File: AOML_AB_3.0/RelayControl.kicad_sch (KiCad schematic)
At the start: 52 parts, among them IC1 CD4043BDR, IC2 CD4043BDR, J5 Conn_01x03, K1 TX2-L2-5V, K10 TX2-L2-5V, K11 TX2-L2-5V, K13 TX2-L2-5V, K2 TX2-L2-5V, K3 TX2-L2-5V, K4 TX2-L2-5V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

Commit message: New reorganization on relay drivers and microcontroller pins
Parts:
- removed TP5: B, TestPoint:TestPoint_Pad_1.0x1.0mm, symbol Connector:TestPoint
- removed TP5: C, TestPoint:TestPoint_Pad_1.0x1.0mm, symbol Connector:TestPoint
- removed TP5: A, TestPoint:TestPoint_Pad_1.0x1.0mm, symbol Connector:TestPoint
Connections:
- net Reset1: now also U5.10 (O7); no longer U5.12 (O5)
- net relay_cal_cont: now also RN3.4 (R3), U5.4 (I4); no longer RN3.6 (R5), U5.3 (I3)
- net relay_cal_res: now also RN3.7 (R6), U5.5 (I5); no longer RN3.5 (R4), U5.4 (I4)
- net relay_gnd_cond: now also RN3.8 (R7), U5.3 (I3); no longer RN3.7 (R6), U5.2 (I2)
- net relay_reset1: now also RN1.6 (R5), U5.7 (I7); no longer RN3.4 (R3), U5.5 (I5)
- net relay_reset2: now also RN3.5 (R4); no longer RN3.3 (R2)
- net relay_reset3: now also RN3.6 (R5); no longer RN3.2 (R1)
- net relay_xbt1: now also RN1.5 (R4), U5.6 (I6); no longer RN1.9 (R8), U5.1 (I1)
- net relay_xbt2: now also RN1.7 (R6), U5.5 (I5); no longer RN1.8 (R7), U5.2 (I2)
- net relay_xbt3: now also RN1.4 (R3), U5.4 (I4); no longer RN1.7 (R6), U5.3 (I3)
- net relay_xbt4: now also RN1.8 (R7), U5.3 (I3); no longer RN1.6 (R5), U5.4 (I4)
- net relay_xbt5: now also RN1.3 (R2), U5.2 (I2); no longer RN1.5 (R4), U5.5 (I5)
- net relay_xbt6: now also RN1.2 (R1), U5.1 (I1); no longer RN1.4 (R3), U5.6 (I6)
- net relay_xbt7: now also RN3.2 (R1), U5.1 (I1); no longer RN1.3 (R2), U5.7 (I7)
- net relay_xbt8: now also RN3.3 (R2), U5.2 (I2); no longer RN3.8 (R7), U5.1 (I1)
- net at K13.6 (-_1): now also U5.12 (O5); no longer U5.13 (O4)
- net at K11.6 (-_1): now also U5.13 (O4); no longer U5.14 (O3)
- net at K10.6 (-_1), K9.6 (-_1): now also U5.14 (O3); no longer U5.15 (O2)
- net at K8.6 (-_1): now also U5.15 (O2); no longer U5.16 (O1)
- net at K7.6 (-_1): now also U5.16 (O1); no longer U5.10 (O7)
- no-connect marks 27 -> 26

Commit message: PCB finished, next BOM
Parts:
- RN2, RN4: Digikey https://www.digikey.com/en/products/detail/yageo/YC124-JR-0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 -> https://www.digikey.com/en/products/detail/yageo/YC164-JR-1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
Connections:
- no-connect marks 26 -> 27
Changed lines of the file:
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@@
   (no_connect (at 119.38 111.76))
   (no_connect (at 149.86 251.46))
+  (no_connect (at 54.61 180.34))
   (no_connect (at 149.86 111.76))
   (no_connect (at 119.38 219.71))
@@
       (effects (font (size 1.27 1.27)) hide)
     )
-    (property "Digikey" "https://www.digikey.com/en/products/detail/yageo/YC124-JR-0710KL/1005019" (at 311.15 222.25 0)
+    (property "Digikey" "https://www.digikey.com/en/products/detail/yageo/YC164-JR-1310KL/17023153?s=N4IgTCBcDaIJ4GMCMA2ALAWgFYCcNIGYkAGAawBsQBdAXyA" (at 311.15 222.25 0)
       (effects (font (size 1.27 1.27)) hide)
     )
@@
       (effects (font (size 1.27 1.27)) hide)
     )
-    (property "Digikey" "https://www.digikey.com/en/products/detail/yageo/YC124-JR-0710KL/1005019" (at 311.15 135.89 0)
+    (property "Digikey" "https://www.digikey.com/en/products/detail/yageo/YC164-JR-1310KL/17023153?s=N4IgTCBcDaIJ4GMCMA2ALAWgFYCcNIGYkAGAawBsQBdAXyA" (at 311.15 135.89 0)
       (effects (font (size 1.27 1.27)) hide)
     )

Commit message: PCB finished, BOM finished
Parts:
- K1, K10, K11, K13, K2, K3, K4, K5, K7, K8, K9: Digikey (none) -> https://www.digikey.com/en/products/detail/panasonic-electr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; Manufacturer_Name Panasonic -> (none); Manufacturer_Part_Number TX2-L2-5V -> (none); Mouser Part Number 769-TX2-L2-5V -> (none); Mouser Price/Stock https://www.mouser.co.uk/ProductDetail/Panasonic-Industrial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 -> (none)

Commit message: PCB finished ready to order (no fiducials for assembly), BOM finished
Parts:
- IC1, IC2: Cost (none) -> 0.49; Part (none) -> CD4043BDR
- J5: Cost (none) -> 1.27; Part (none) -> 0436500315
- K1, K10, K11, K13, K2, K3, K4, K5, K7, K8, K9: Cost (none) -> 3.61; Part (none) -> TX2-L2-5V
- K6: Cost (none) -> 3.61; Digikey (none) -> https://www.digikey.com/en/products/detail/panasonic-electr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; Manufacturer_Name Panasonic -> (none); Manufacturer_Part_Number TX2-L2-5V -> (none); Mouser Part Number 769-TX2-L2-5V -> (none); Mouser Price/Stock https://www.mouser.co.uk/ProductDetail/Panasonic-Industrial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 -> (none); Part (none) -> TX2-L2-5V
- R1: Cost (none) -> 0.1; Part (none) -> RC0805FR-10330RL
- R10: Cost (none) -> 38.87; Part (none) -> Y14535K00000V9L
- R11: Cost (none) -> 0.1; Part (none) -> CFR-25JR-52-15K
- RN1, RN3: Cost (none) -> 0.14; Part (none) -> YC158TJR-0710KL
- RN2, RN4: Cost (none) -> 0.1; Part (none) -> YC164-JR-1310KL
- U10, U11, U12, U13, U14, U15, U16, U17: Cost (none) -> 1.28; Part (none) -> TLP170AM(TPL,E
- U5: Cost (none) -> 0.46; Part (none) -> ULN2003ADR

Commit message: PCB v2 started to make changes after meeting w/P.P & Z.B. - XBT connectors, AXR ABC and MUX GPS Tx
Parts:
- J5: footprint Molex_3x1_0436500315:CON_436500315_MOL -> CUI_3x1_connector:CUI_TBP02R2-381-03BE; Cost 1.27 -> 0.58; Digikey https://www.digikey.com/en/products/detail/molex/0436500315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 -> https://www.digikey.com/en/products/detail/cui-devices/TBP0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; Part 0436500315 -> TBP02R2-381-03BE
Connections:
- net XBT1_A: now also J5.3 (Pin_3); no longer J5.1 (Pin_1)
- net XBT1_C: now also J5.1 (Pin_1); no longer J5.3 (Pin_3)
- net XBT2_A: now also J5.3 (Pin_3); no longer J5.1 (Pin_1)
- net XBT2_C: now also J5.1 (Pin_1); no longer J5.3 (Pin_3)
- net XBT3_A: now also J5.3 (Pin_3); no longer J5.1 (Pin_1)
- net XBT3_C: now also J5.1 (Pin_1); no longer J5.3 (Pin_3)
- net XBT4_A: now also J5.3 (Pin_3); no longer J5.1 (Pin_1)
- net XBT4_C: now also J5.1 (Pin_1); no longer J5.3 (Pin_3)
- net XBT5_A: now also J5.3 (Pin_3); no longer J5.1 (Pin_1)
- net XBT5_C: now also J5.1 (Pin_1); no longer J5.3 (Pin_3)
- net XBT6_A: now also J5.3 (Pin_3); no longer J5.1 (Pin_1)
- net XBT6_C: now also J5.1 (Pin_1); no longer J5.3 (Pin_3)
- net XBT7_A: now also J5.3 (Pin_3); no longer J5.1 (Pin_1)
- net XBT7_C: now also J5.1 (Pin_1); no longer J5.3 (Pin_3)
- net XBT8_A: now also J5.3 (Pin_3); no longer J5.1 (Pin_1)
- net XBT8_C: now also J5.1 (Pin_1); no longer J5.3 (Pin_3)

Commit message: New version v3, in assembly process and noting changes for next revision
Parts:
- removed RN1, RN3: 10k, Resistor_network-10k:SMT_JR-0710KL_YAG, symbol Device:R_Network08
- added RN1, RN3: 746X101103JP, Network_resistor_10k_bussed:746X101103JP-3, symbol Network_resistor_10k_bussed:746X101103JP
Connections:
- net GND: now also RN1.10, RN1.5, RN3.10, RN3.5
- net relay_cal_cont: now also RN3.1
- net relay_cal_res: now also RN3.6
- net relay_gnd_cond: now also RN3.2
- net relay_reset1: now also RN1.7
- net relay_reset2: now also RN3.8
- net relay_reset3: now also RN3.7
- net relay_xbt1: now also RN1.8
- net relay_xbt2: now also RN1.6
- net relay_xbt3: now also RN1.1
- net relay_xbt4: now also RN1.2
- net relay_xbt5: now also RN1.3
- net relay_xbt6: now also RN1.4
- net relay_xbt7: now also RN3.4
- net relay_xbt8: now also RN3.3

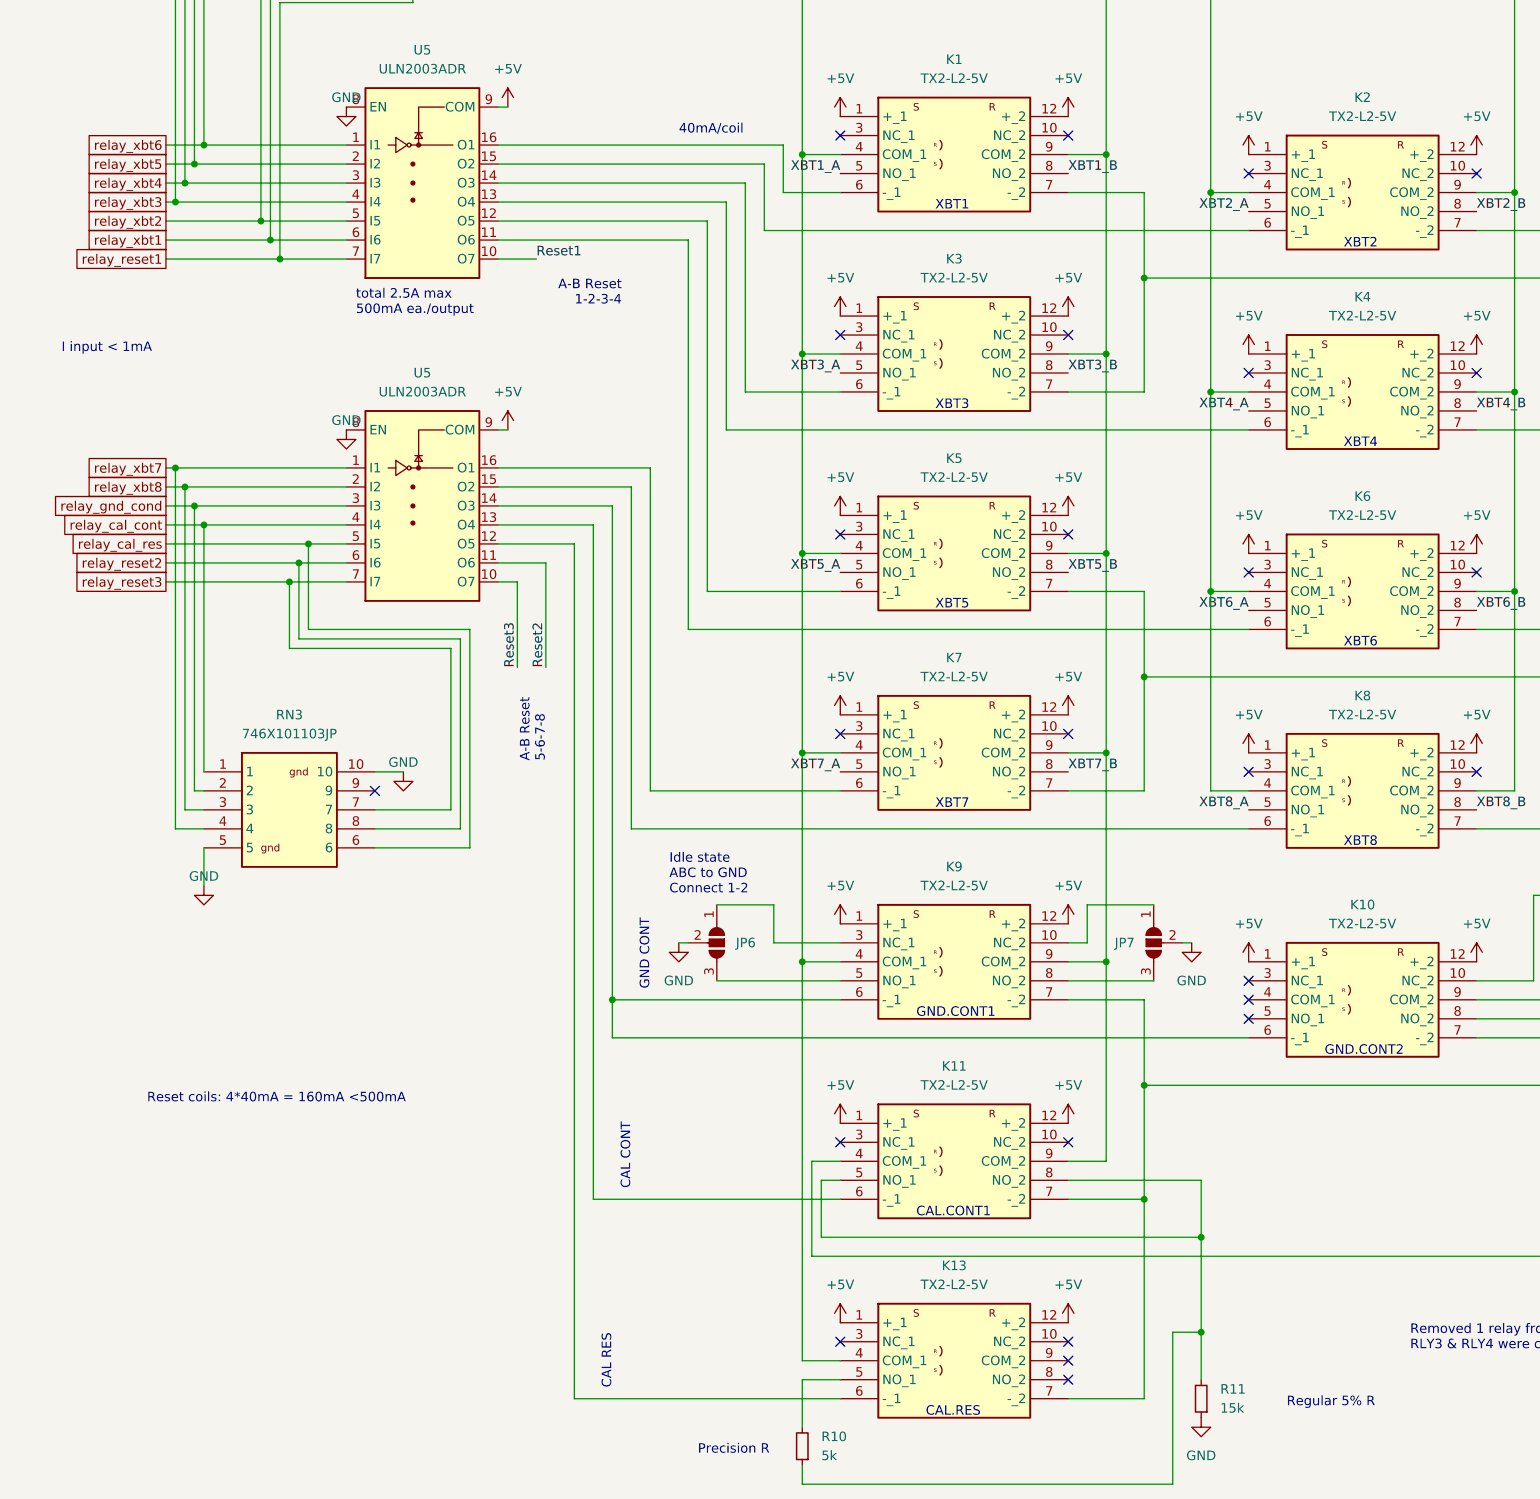
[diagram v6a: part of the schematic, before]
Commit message: Board V3.0 rev3 completed: several footprints fixed, added mosfet inverter to GPS data input, buffer to Vin measurement, jumper to 12V motor supply bus, and made power rails wider
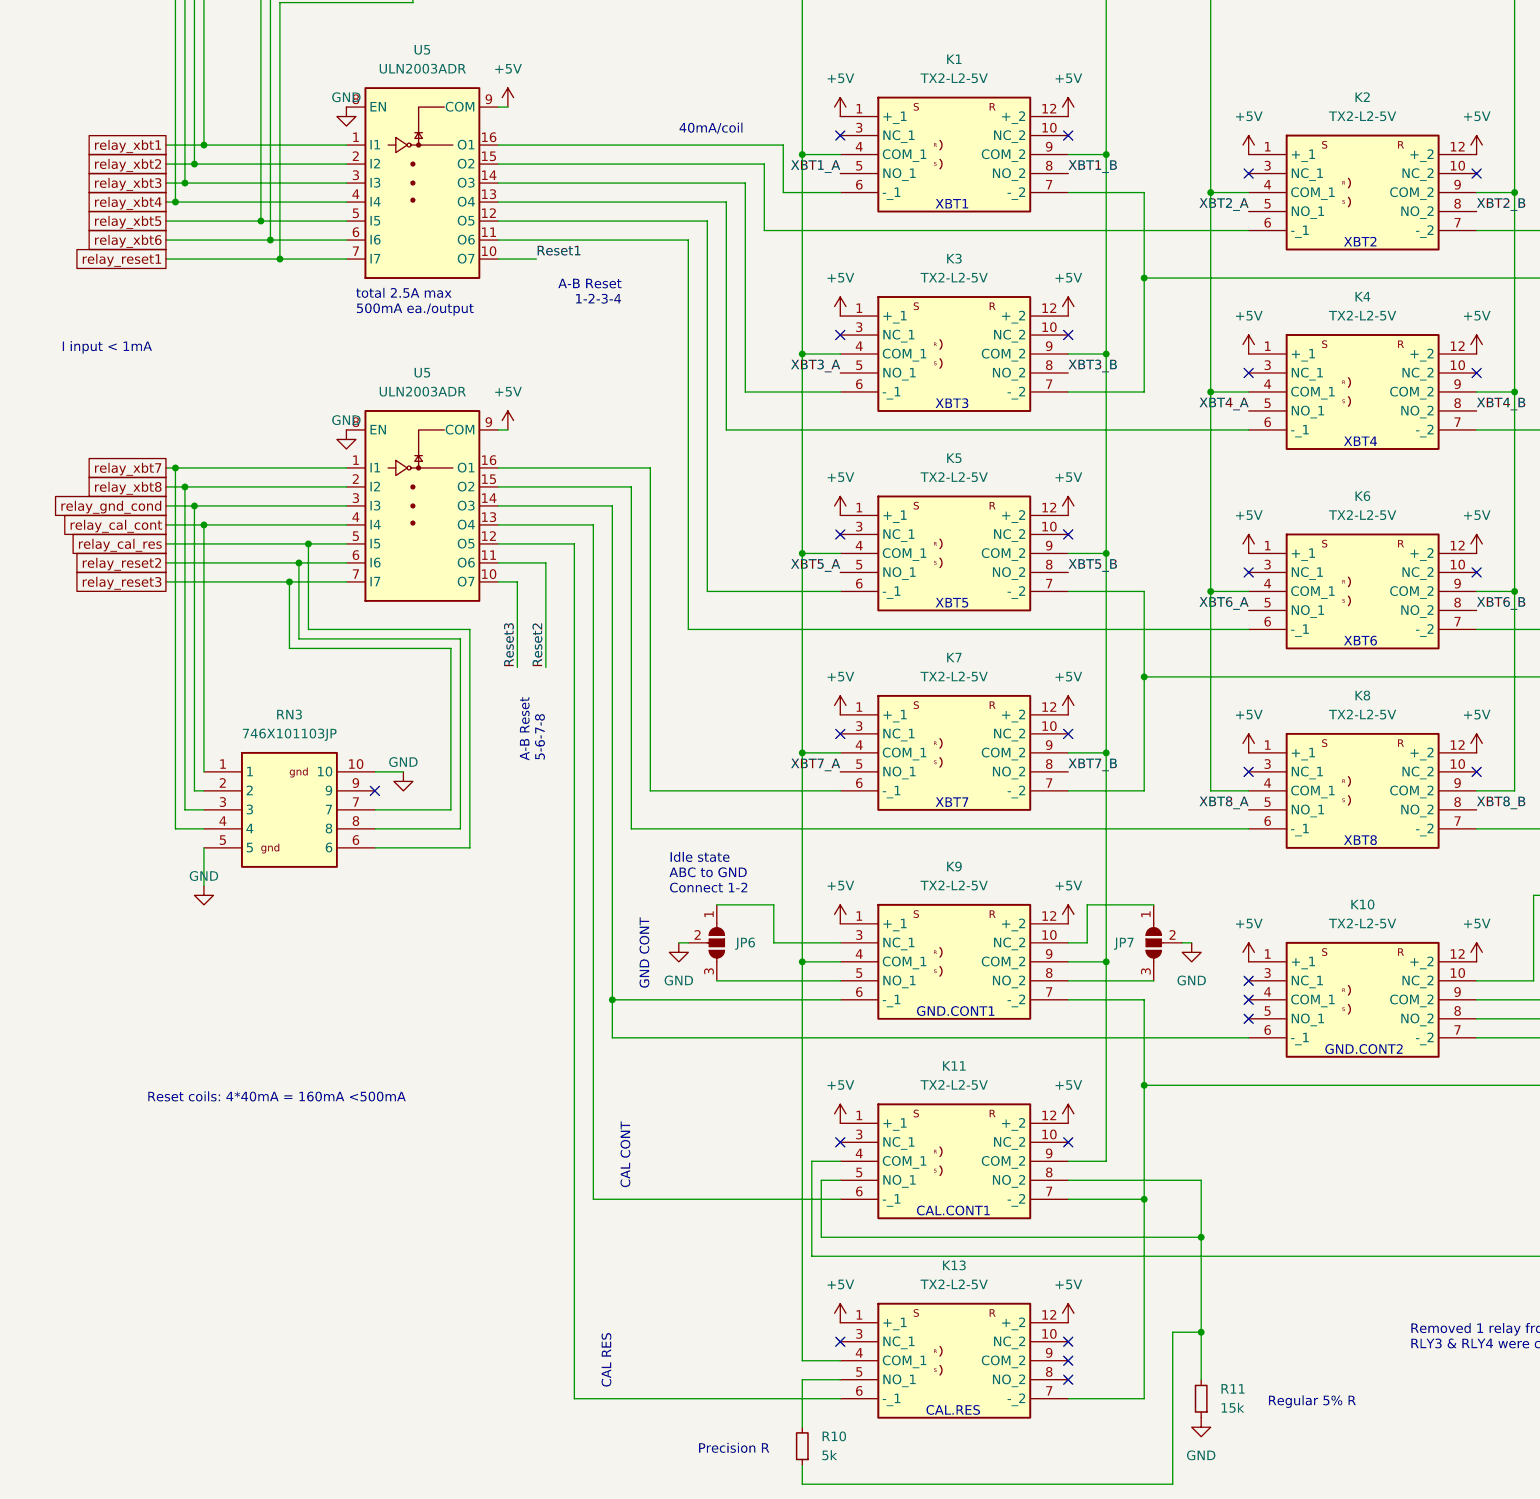
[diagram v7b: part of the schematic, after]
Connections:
- net relay_xbt1: now also RN1.4, U5.1 (I1); no longer RN1.8, U5.6 (I6)
- net relay_xbt2: now also RN1.3, U5.2 (I2); no longer RN1.6, U5.5 (I5)
- net relay_xbt3: now also RN1.2, U5.3 (I3); no longer RN1.1, U5.4 (I4)
- net relay_xbt4: now also RN1.1, U5.4 (I4); no longer RN1.2, U5.3 (I3)
- net relay_xbt5: now also RN1.6, U5.5 (I5); no longer RN1.3, U5.2 (I2)
- net relay_xbt6: now also RN1.8, U5.6 (I6); no longer RN1.4, U5.1 (I1)
